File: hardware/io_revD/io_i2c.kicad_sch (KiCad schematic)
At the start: 49 parts, among them J1 Target Interface, 2716 Pinout, J2 Jumper Block, J3 Jumper Block, J4 Target Interface, 2716 Pinout, Q1 2N7000, U1 2716, U2 74HCT74, U3 74HCT125, U4 74HCT138, U6 MCP23018-E_SP, U7 74HCT138

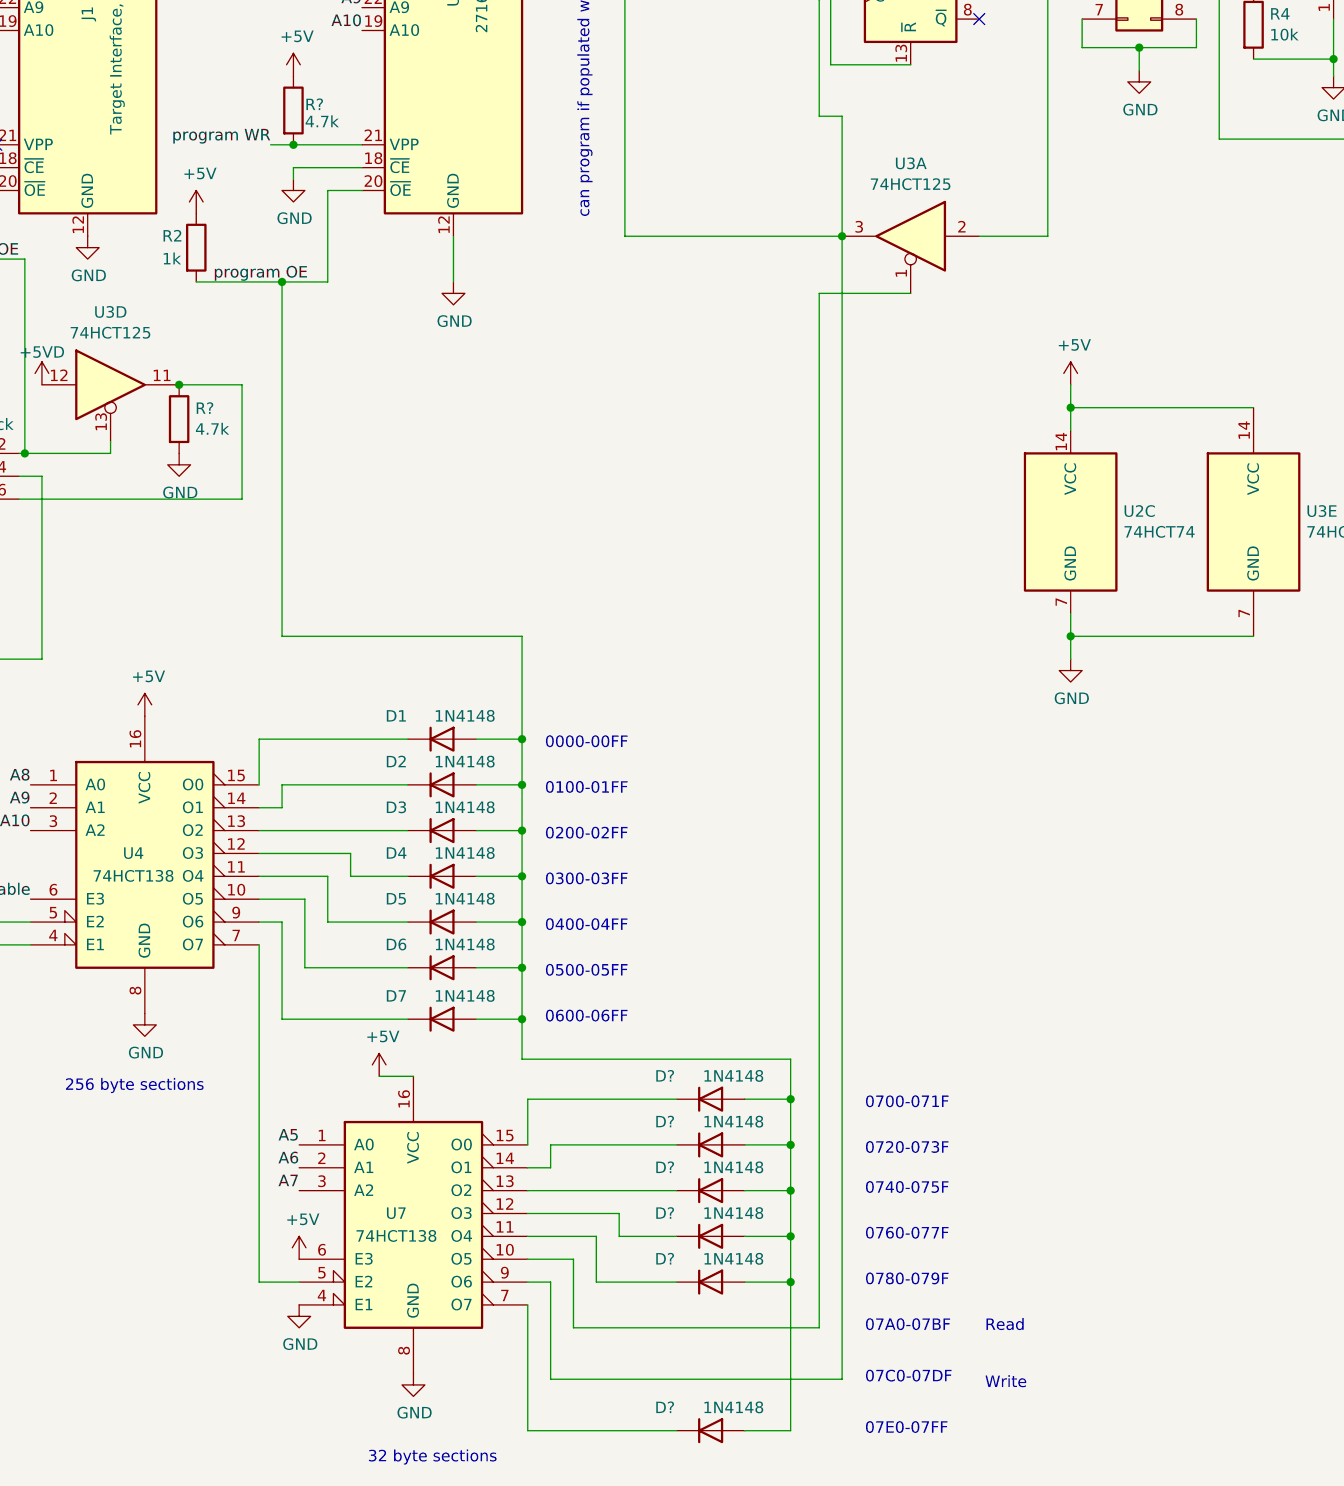
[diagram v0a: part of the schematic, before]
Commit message: added diode for programming
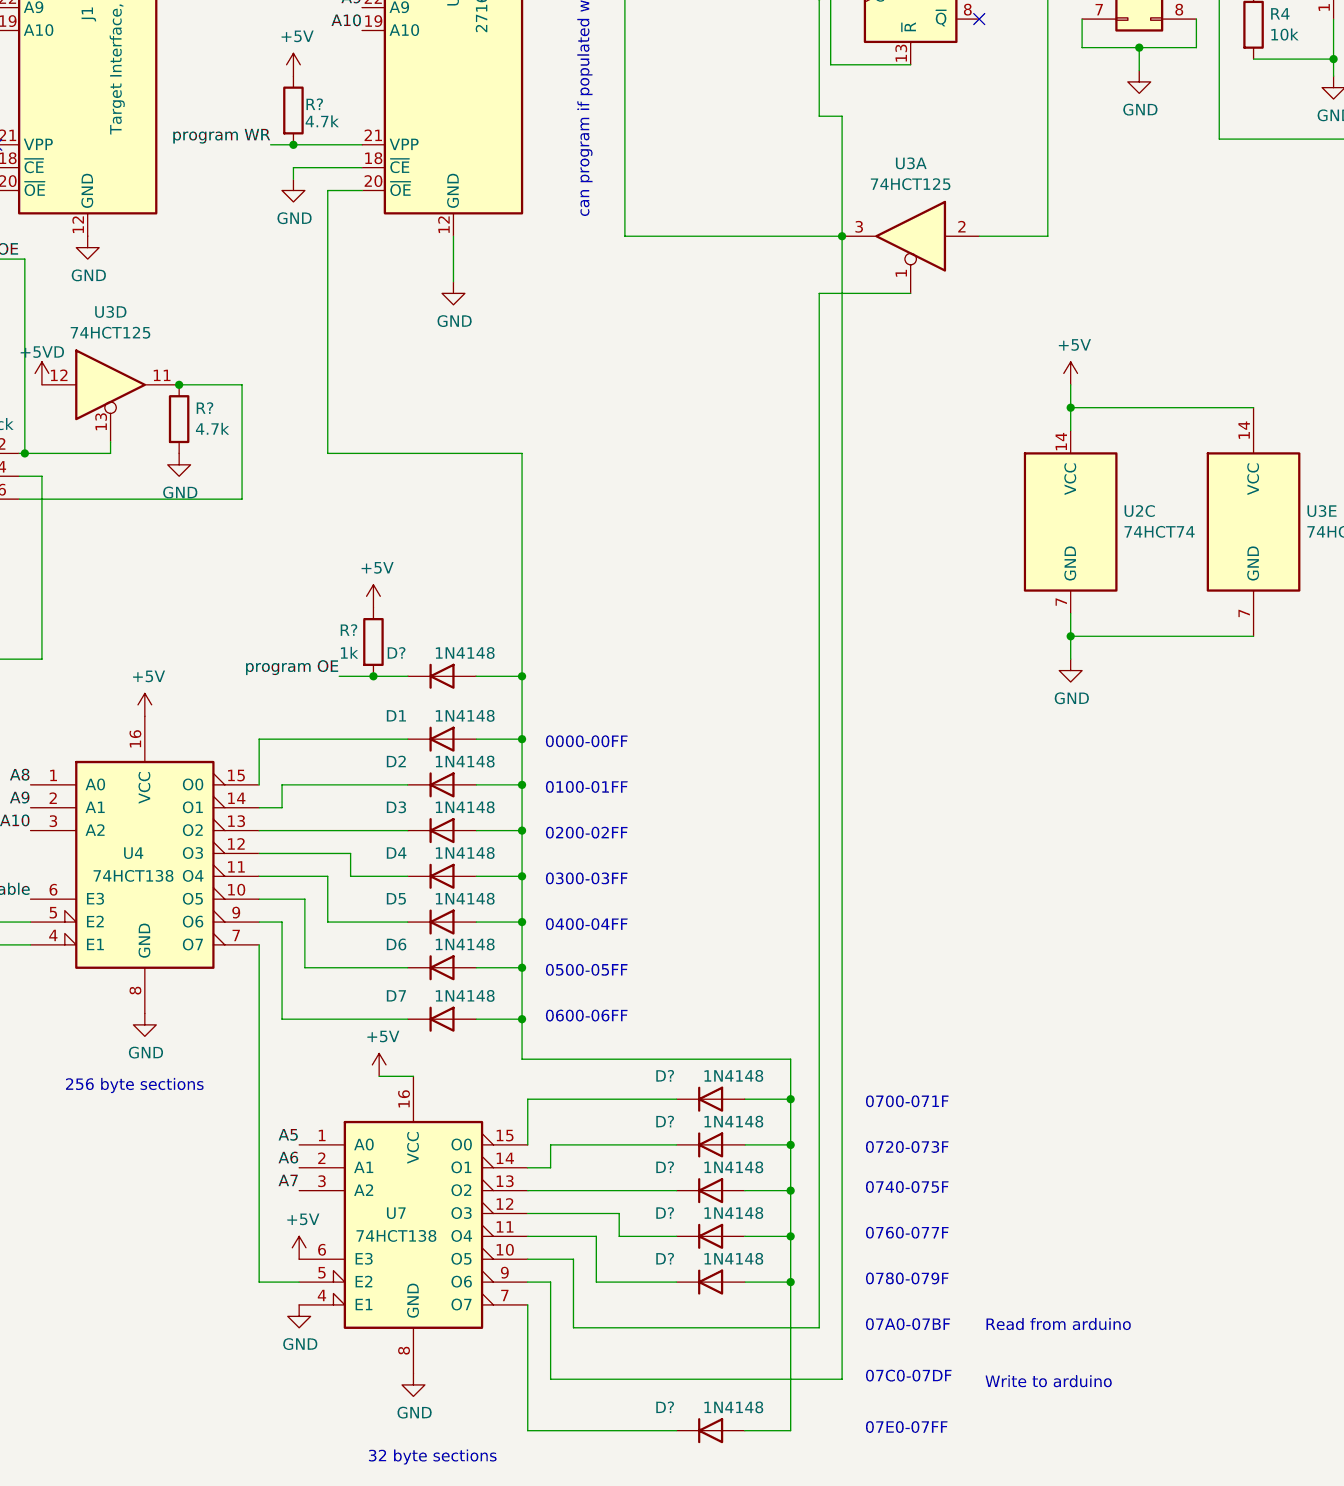
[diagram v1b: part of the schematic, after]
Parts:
- removed R2: 1k, Resistor_THT:R_Axial_DIN0207_L6.3mm_D2.5mm_P2.54mm_Vertical, symbol Device:R
- added D?: 1N4148, Diode_THT:D_DO-35_SOD27_P2.54mm_Vertical_AnodeUp, symbol Diode:1N4148
- added R?: 1k, Resistor_THT:R_Axial_DIN0207_L6.3mm_D2.5mm_P2.54mm_Vertical, symbol Device:R
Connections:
- net +5V: now also R?.1
- net program OE: now also D?.1 (K), R?.2; no longer D1.2 (A), D2.2 (A), D3.2 (A), D4.2 (A), D5.2 (A), D6.2 (A), D7.2 (A), D?.2 (A), D?.2 (A), D?.2 (A), D?.2 (A), D?.2 (A), D?.2 (A), U1.20 (~{OE})
- new net: D1.2 (A), D2.2 (A), D3.2 (A), D4.2 (A), D5.2 (A), D6.2 (A), D7.2 (A), D?.2 (A), D?.2 (A), D?.2 (A), D?.2 (A), D?.2 (A), D?.2 (A), D?.2 (A), U1.20 (~{OE})
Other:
- note added: "Read from arduino"
- note added: "Write to arduino"
- note removed: "Read"
- note removed: "Write"
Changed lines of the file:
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@@
   (junction (at 184.15 88.265) (diameter 0) (color 0 0 0 0)
   )
+  (junction (at 151.13 163.83) (diameter 0) (color 0 0 0 0)
+  )
   (junction (at 252.73 93.345) (diameter 0) (color 0 0 0 0)
   )
@@
   (junction (at 180.975 215.9) (diameter 0) (color 0 0 0 0)
   )
-  (junction (at 124.46 120.015) (diameter 0) (color 0 0 0 0)
-  )
   (junction (at 212.09 133.985) (diameter 0) (color 0 0 0 0)
   )
@@
   )
   (junction (at 185.42 80.645) (diameter 0) (color 0 0 0 0)
+  )
+  (junction (at 134.62 163.83) (diameter 0) (color 0 0 0 0)
   )
   (junction (at 212.09 159.385) (diameter 0) (color 0 0 0 0)
@@
     (stroke (width 0) (type default) (color 0 0 0 0))
   )
-  (wire (pts (xy 124.46 159.385) (xy 124.46 120.015))
+  (wire (pts (xy 129.54 109.855) (xy 129.54 139.065))
     (stroke (width 0) (type default) (color 0 0 0 0))
   )
@@
     (stroke (width 0) (type default) (color 0 0 0 0))
   )
+  (wire (pts (xy 151.13 163.83) (xy 151.13 170.815))
+    (stroke (width 0) (type default) (color 0 0 0 0))
+  )
   (wire (pts (xy 234.95 41.275) (xy 234.95 42.545))
     (stroke (width 0) (type default) (color 0 0 0 0))
@@
     (stroke (width 0) (type default) (color 0 0 0 0))
   )
-  (wire (pts (xy 151.13 159.385) (xy 151.13 170.815))
+  (wire (pts (xy 151.13 139.065) (xy 151.13 163.83))
     (stroke (width 0) (type default) (color 0 0 0 0))
   )
@@
     (stroke (width 0) (type default) (color 0 0 0 0))
   )
+  (wire (pts (xy 146.05 163.83) (xy 151.13 163.83))
+    (stroke (width 0) (type default) (color 0 0 0 0))
+  )
   (wire (pts (xy 132.08 31.115) (xy 142.875 31.115))
     (stroke (width 0) (type default) (color 0 0 0 0))
@@
     (stroke (width 0) (type default) (color 0 0 0 0))
   )
-  (wire (pts (xy 114.935 120.015) (xy 124.46 120.015))
+  (wire (pts (xy 130.81 163.83) (xy 134.62 163.83))
     (stroke (width 0) (type default) (color 0 0 0 0))
   )
@@
     (stroke (width 0) (type default) (color 0 0 0 0))
   )
+  (wire (pts (xy 134.62 163.83) (xy 138.43 163.83))
+    (stroke (width 0) (type default) (color 0 0 0 0))
+  )
   (wire (pts (xy 153.67 66.675) (xy 162.56 66.675))
     (stroke (width 0) (type default) (color 0 0 0 0))
@@
     (stroke (width 0) (type default) (color 0 0 0 0))
   )
-  (wire (pts (xy 124.46 159.385) (xy 151.13 159.385))
+  (wire (pts (xy 129.54 139.065) (xy 151.13 139.065))
     (stroke (width 0) (type default) (color 0 0 0 0))
   )
@@
     (stroke (width 0) (type default) (color 0 0 0 0))
   )
-  (wire (pts (xy 124.46 120.015) (xy 129.54 120.015))
-    (stroke (width 0) (type default) (color 0 0 0 0))
-  )
   (wire (pts (xy 180.975 210.82) (xy 180.975 215.9))
     (stroke (width 0) (type default) (color 0 0 0 0))
@@
     (stroke (width 0) (type default) (color 0 0 0 0))
   )
-  (wire (pts (xy 129.54 109.855) (xy 129.54 120.015))
-    (stroke (width 0) (type default) (color 0 0 0 0))
-  )
   (wire (pts (xy 125.73 104.775) (xy 133.35 104.775))
     (stroke (width 0) (type default) (color 0 0 0 0))
@@
     (effects (font (size 1.27 1.27)) (justify left bottom))
   )
-  (text "Read" (at 202.565 236.855 0)
+  (text "Read from arduino" (at 202.565 236.855 0)
     (effects (font (size 1.27 1.27)) (justify left bottom))
   )
@@
     (effects (font (size 1.27 1.27)) (justify left bottom))
   )
-  (text "Write" (at 202.565 243.205 0)
+  (text "Write to arduino" (at 202.565 243.205 0)
     (effects (font (size 1.27 1.27)) (justify left bottom))
   )
@@
     (effects (font (size 1.27 1.27)) (justify right bottom))
   )
+  (label "program OE" (at 130.81 163.83 180)
+    (effects (font (size 1.27 1.27)) (justify right bottom))
+  )
   (label "138 enable" (at 96.52 188.595 180)
     (effects (font (size 1.27 1.27)) (justify right bottom))
@@
   (label "SCL" (at 268.605 95.885 180)
     (effects (font (size 1.27 1.27)) (justify right bottom))
-  )
-  (label "program OE" (at 116.84 120.015 0)
-    (effects (font (size 1.27 1.27)) (justify left bottom))
   )
   (label "A8" (at 96.52 175.895 180)
@@
     )
     (property "Datasheet" "" (id 3) (at 109.22 201.295 0)
-      (effects (font (size 1.27 1.27)) hide)
-    )
-    (pin "1")
-  )
-  (symbol (lib_id "Device:R") (at 114.935 116.205 0) (unit 1)
-    (in_bom yes) (on_board yes)
-    (property "Reference" "R2" (id 0) (at 111.125 114.935 0)
-      (effects (font (size 1.27 1.27)) (justify left))
-    )
-    (property "Value" "1k" (id 1) (at 111.125 117.475 0)
-      (effects (font (size 1.27 1.27)) (justify left))
-    )
-    (property "Footprint" "Resistor_THT:R_Axial_DIN0207_L6.3mm_D2.5mm_P2.54mm_Vertical" (id 2) (at 113.157 116.205 90)
-      (effects (font (size 1.27 1.27)) hide)
-    )
-    (property "Datasheet" "~" (id 3) (at 114.935 116.205 0)
-      (effects (font (size 1.27 1.27)) hide)
-    )
-    (pin "1")
-    (pin "2")
-  )
-  (symbol (lib_id "power:+5V") (at 114.935 112.395 0) (unit 1)
-    (in_bom yes) (on_board yes)
-    (property "Reference" "#PWR0127" (id 0) (at 114.935 116.205 0)
-      (effects (font (size 1.27 1.27)) hide)
-    )
-    (property "Value" "+5V" (id 1) (at 115.316 108.0008 0))
-    (property "Footprint" "" (id 2) (at 114.935 112.395 0)
-      (effects (font (size 1.27 1.27)) hide)
-    )
-    (property "Datasheet" "" (id 3) (at 114.935 112.395 0)
       (effects (font (size 1.27 1.27)) hide)
     )
@@
     (pin "1")
   )
+  (symbol (lib_id "power:+5V") (at 134.62 156.21 0) (unit 1)
+    (in_bom yes) (on_board yes)
+    (property "Reference" "#PWR?" (id 0) (at 134.62 160.02 0)
+      (effects (font (size 1.27 1.27)) hide)
+    )
+    (property "Value" "+5V" (id 1) (at 135.001 151.8158 0))
+    (property "Footprint" "" (id 2) (at 134.62 156.21 0)
+      (effects (font (size 1.27 1.27)) hide)
+    )
+    (property "Datasheet" "" (id 3) (at 134.62 156.21 0)
+      (effects (font (size 1.27 1.27)) hide)
+    )
+    (pin "1")
+  )
   (symbol (lib_id "74xx:74LS125") (at 43.815 76.2 0) (unit 2)
     (in_bom yes) (on_board yes)
@@
     )
     (pin "1")
+  )
+  (symbol (lib_id "Device:R") (at 134.62 160.02 0) (unit 1)
+    (in_bom yes) (on_board yes)
+    (property "Reference" "R?" (id 0) (at 130.81 158.75 0)
+      (effects (font (size 1.27 1.27)) (justify left))
+    )
+    (property "Value" "1k" (id 1) (at 130.81 161.29 0)
+      (effects (font (size 1.27 1.27)) (justify left))
+    )
+    (property "Footprint" "Resistor_THT:R_Axial_DIN0207_L6.3mm_D2.5mm_P2.54mm_Vertical" (id 2) (at 132.842 160.02 90)
+      (effects (font (size 1.27 1.27)) hide)
+    )
+    (property "Datasheet" "~" (id 3) (at 134.62 160.02 0)
+      (effects (font (size 1.27 1.27)) hide)
+    )
+    (pin "1")
+    (pin "2")
   )
   (symbol (lib_id "Device:R") (at 232.41 91.44 0) (unit 1)
@@
     (pin "1")
   )
+  (symbol (lib_id "Diode:1N4148") (at 142.24 163.83 0) (unit 1)
+    (in_bom yes) (on_board yes)
+    (property "Reference" "D?" (id 0) (at 137.16 161.29 0))
+    (property "Value" "1N4148" (id 1) (at 144.78 161.29 0))
+    (property "Footprint" "Diode_THT:D_DO-35_SOD27_P2.54mm_Vertical_AnodeUp" (id 2) (at 142.24 168.275 0)
+      (effects (font (size 1.27 1.27)) hide)
+    )
+    (property "Datasheet" "https://assets.nexperia.com/documents/data-sheet/1N4148_1N4448.pdf" (id 3) (at 142.24 163.83 0)
+      (effects (font (size 1.27 1.27)) hide)
+    )
+    (pin "1")
+    (pin "2")
+  )
   (symbol (lib_id "Diode:1N4004") (at 211.455 41.91 180) (unit 1)
     (in_bom yes) (on_board yes) (fields_autoplaced)
@@
       (reference "#PWR0126") (unit 1) (value "GND") (footprint "")
     )
-    (path "/00000000-0000-0000-0000-000060a45b63"
-      (reference "#PWR0127") (unit 1) (value "+5V") (footprint "")
-    )
     (path "/00000000-0000-0000-0000-000061057962"
       (reference "#PWR0128") (unit 1) (value "+5V") (footprint "")
@@
       (reference "#PWR?") (unit 1) (value "GND") (footprint "")
     )
+    (path "/1f6a280c-02f7-41a2-af9f-44fb04f0a9b2"
+      (reference "#PWR?") (unit 1) (value "+5V") (footprint "")
+    )
     (path "/43879ac7-f230-4696-95ed-6babb22f0407"
       (reference "#PWR?") (unit 1) (value "+5V") (footprint "")
@@
       (reference "D?") (unit 1) (value "1N4148") (footprint "Diode_THT:D_DO-35_SOD27_P2.54mm_Vertical_AnodeUp")
     )
+    (path "/eababe2a-0ecd-4427-a6f7-2ec75821d4fc"
+      (reference "D?") (unit 1) (value "1N4148") (footprint "Diode_THT:D_DO-35_SOD27_P2.54mm_Vertical_AnodeUp")
+    )
     (path "/f8f23bc7-7f9a-45bb-bcc9-d7c30e1a0b2d"
       (reference "D?") (unit 1) (value "1N4148") (footprint "Diode_THT:D_DO-35_SOD27_P2.54mm_Vertical_AnodeUp")
@@
       (reference "R1") (unit 1) (value "4.7k") (footprint "Resistor_THT:R_Axial_DIN0207_L6.3mm_D2.5mm_P2.54mm_Vertical")
     )
-    (path "/00000000-0000-0000-0000-000060a45b5d"
-      (reference "R2") (unit 1) (value "1k") (footprint "Resistor_THT:R_Axial_DIN0207_L6.3mm_D2.5mm_P2.54mm_Vertical")
-    )
     (path "/88ce3174-a8b3-4149-886a-872ed4746e98"
       (reference "R4") (unit 1) (value "10k") (footprint "Resistor_THT:R_Axial_DIN0207_L6.3mm_D2.5mm_P2.54mm_Vertical")
@@
       (reference "R?") (unit 1) (value "4.7k") (footprint "Resistor_THT:R_Axial_DIN0207_L6.3mm_D2.5mm_P2.54mm_Vertical")
     )
+    (path "/857b2b5c-6887-40fa-8781-7287c485d91d"
+      (reference "R?") (unit 1) (value "1k") (footprint "Resistor_THT:R_Axial_DIN0207_L6.3mm_D2.5mm_P2.54mm_Vertical")
+    )
     (path "/00000000-0000-0000-0000-0000607df9f3"
